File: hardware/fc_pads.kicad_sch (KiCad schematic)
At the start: 41 parts, among them J15 5V, J16 5V, J17 GND, J18 GND, J19 ADC2, J20 LED, J21 LED, J22 GND, J23 SCL, J24 5V, J25 5V, J26 SDA, J27 GND, J28 GND, J29 BUZ-, J30 5V, J31 LED, J32 LED, J33 BUZ+, J34 GND, J35 GND, J37 5V, J38 CAM, J39 VTX, J40 GND, J41 10V, J42 4V5, J43 GND, J44 PIO_TX0, J45 PIO_RX0, J46 NC, J47 NC, J48 RX0, J49 TX0, J50 GND, J51 GND, J52 4V5, J53 GND, J54 TX1, J55 RX1, U12 SM06B-SRSS-TB(LF)(SN)

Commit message: Schematic readability: TP texts, C19/C107, C26, title blocks (FB5 item 6, V9-V11/M6)
- TestPoint values ('TestPoint') hidden on all sheets: the stacked TP16/TP17
  (root), TP24/TP25 and TP18/TP19/TP26/TP27 (RP2354A) texts no longer overlap.
- C19 reference/value moved left of the part (no longer printed over C107).
- C26 Description field hidden.
- Title blocks: rev r2, date 2026-10 (title added where missing) on the root,
  RP2354A, Power, IMU, OSD, Pads, ESC channel and Core interface sheets.
Edited with kicad-skip, re-saved with `kicad-cli sch upgrade --force` so the
diff stays minimal. Not done: rx_esp32c3_sx1281 and fc_blackbox title blocks
(they carry other projects' instances, OpenRX-Lite / BLACKBOX, and the headless
re-save renumbers their references); TP10 outside the frame (moving it would
detach its wire); N4 SPI0 label lift (label position is the connection point);
M7 net naming (+4v5 / +3.3V vs +3V3) left as is, it touches the LGA spec.
ERC 31 errors (unchanged).

Co-Authored-By: Claude Opus 5.5 <noreply@anthropic.com>
Claude-Session: https://claude.ai/code/session_01KTp3FLjVXfXdWrkmr6af7d
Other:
- title: (none) -> Pads
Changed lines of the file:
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@@
 	(generator_version "10.0")
 	(paper "A4")
+	(title_block
+		(title "Pads")
+		(date "2026-10")
+		(rev "r2")
+	)
 	(polyline
 		(pts

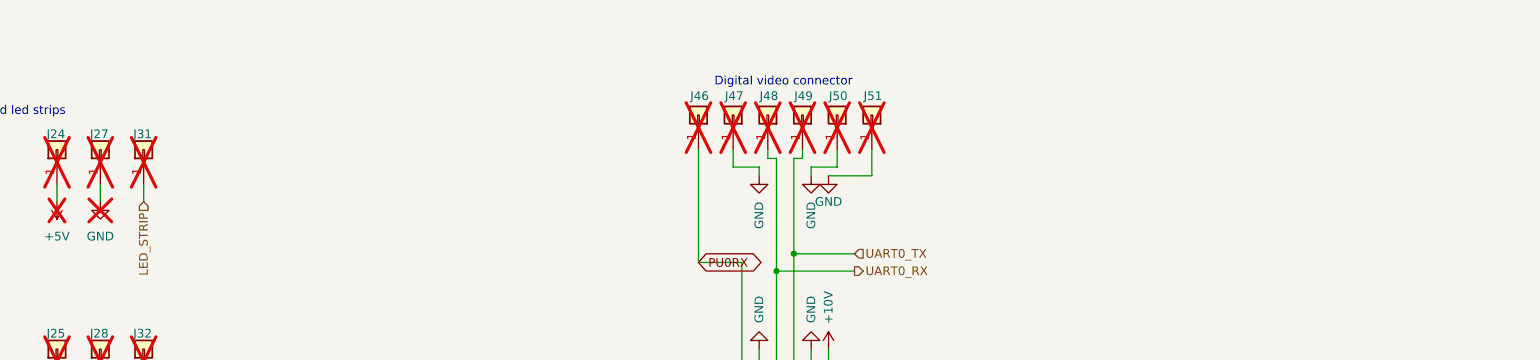
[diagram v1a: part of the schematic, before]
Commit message: One board: merge Base and Core onto the OpenAIO-Whoop 8L HDI stackup
- hardware/OpenAIO.kicad_pcb: the routed Base and Core layouts of 8fa8d7b
  side by side in one board, all routing kept (Core promoted to 8 layers
  before the append so no Base layer was dropped). J90/J91 LGA deleted;
  their 46 nets are now direct links (51 unconnected, listed in
  research/ROUTING.md). Stackup and board setup from OpenAIO-Whoop:
  8L HDI 1+6+1, 0.997 mm, 1 oz all layers, microvia 0.25/0.10,
  buried 0.33/0.15. Base DRC severities and exclusions kept.
- hardware/OpenAIO.kicad_dru: canonical block, Whoop HDI via rules,
  Base/Core rules that still apply; LGA, 2 oz and 1.6 mm via rules gone.
- Schematic: core_interface sheet removed; DPS368 baro U28 on I2C0;
  review fixes (U3 HF cap C116, RP2354 caps C117/C118, buzzer flyback D10,
  SD card on +3.3V, D9 on +4v5, FLASH_CS -> SD_CS, PWR_FLAGs, U7 pin
  names, ESC cap pin types, L4 LCSC). ERC 32 -> 0 errors.
- Libraries project-local: every footprint, 3D model and symbol in lib;
  OPENDRONE_LIB aliases removed from the lib tables.
- Two-board projects, multiboard config and LGA tools removed; Whoop
  board tools added in hardware/tools.
- Docs: README, AGENTS.md, research/ROUTING.md (hand-over),
  SCHEMATIC-REVIEW-2026-10-15.md, Betaflight target baro.

DRC: 38 errors (25 dangling LGA escape vias, 13 Core leftovers listed),
51 unconnected (the Base-Core links), 0 net or value parity issues.

Co-Authored-By: Claude Opus 5.5 <noreply@anthropic.com>
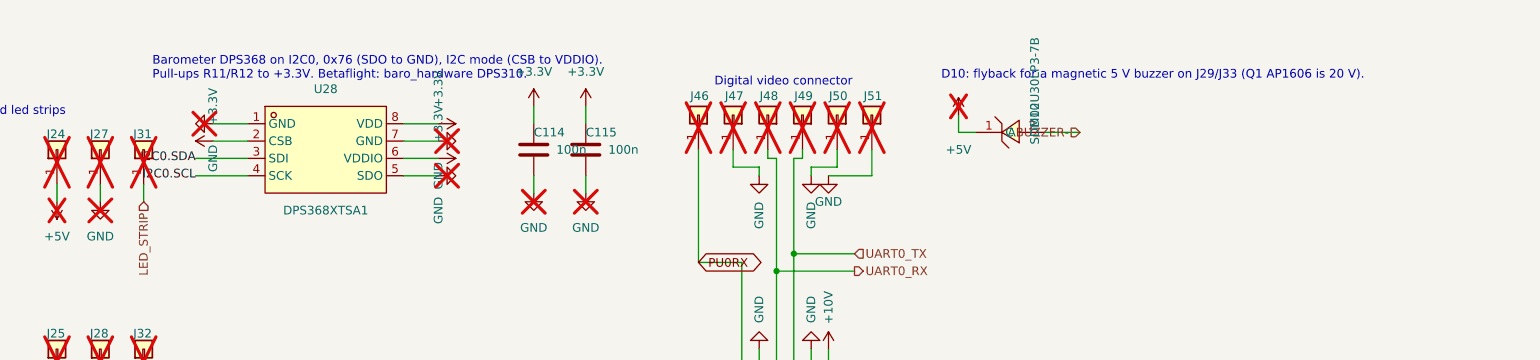
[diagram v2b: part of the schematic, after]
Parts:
- added C114, C115: 100n, lib:C_0201_0603Metric, symbol Device:C
- added D10: SDM02U30LP3-7B, lib:X3-DFN0603-2_L0.6-W0.3-RD, symbol lib:SDM02U30LP3-7B
- added U28: DPS368XTSA1, lib:LGA-8_L2.5-W2.0-P0.65-TR_DPS368, symbol lib:DPS368XTSA1
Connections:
- net +5V: now also D10.1 (C)
- net BUZZER-: now also D10.2 (A)
- net GND: now also C114.2, C115.2, U28.1 (GND), U28.5 (SDO), U28.7 (GND)
- net I2C0.SCL: now also U28.4 (SCK)
- net I2C0.SDA: now also U28.3 (SDI)
- new net +3.3V: C114.1, C115.1, U28.2 (CSB), U28.6 (VDDIO), U28.8 (VDD)
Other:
- note added: "Barometer DPS368 on I2C0, 0x76 (SDO to GND), I2C mode (CSB to VDDIO). Pull-ups R11/R12 to +3.3V. Betaflight: baro_hardware DPS310."
- note added: "D10: flyback for a magnetic 5 V buzzer on J29/J33 (Q1 AP1606 is 20 V)."

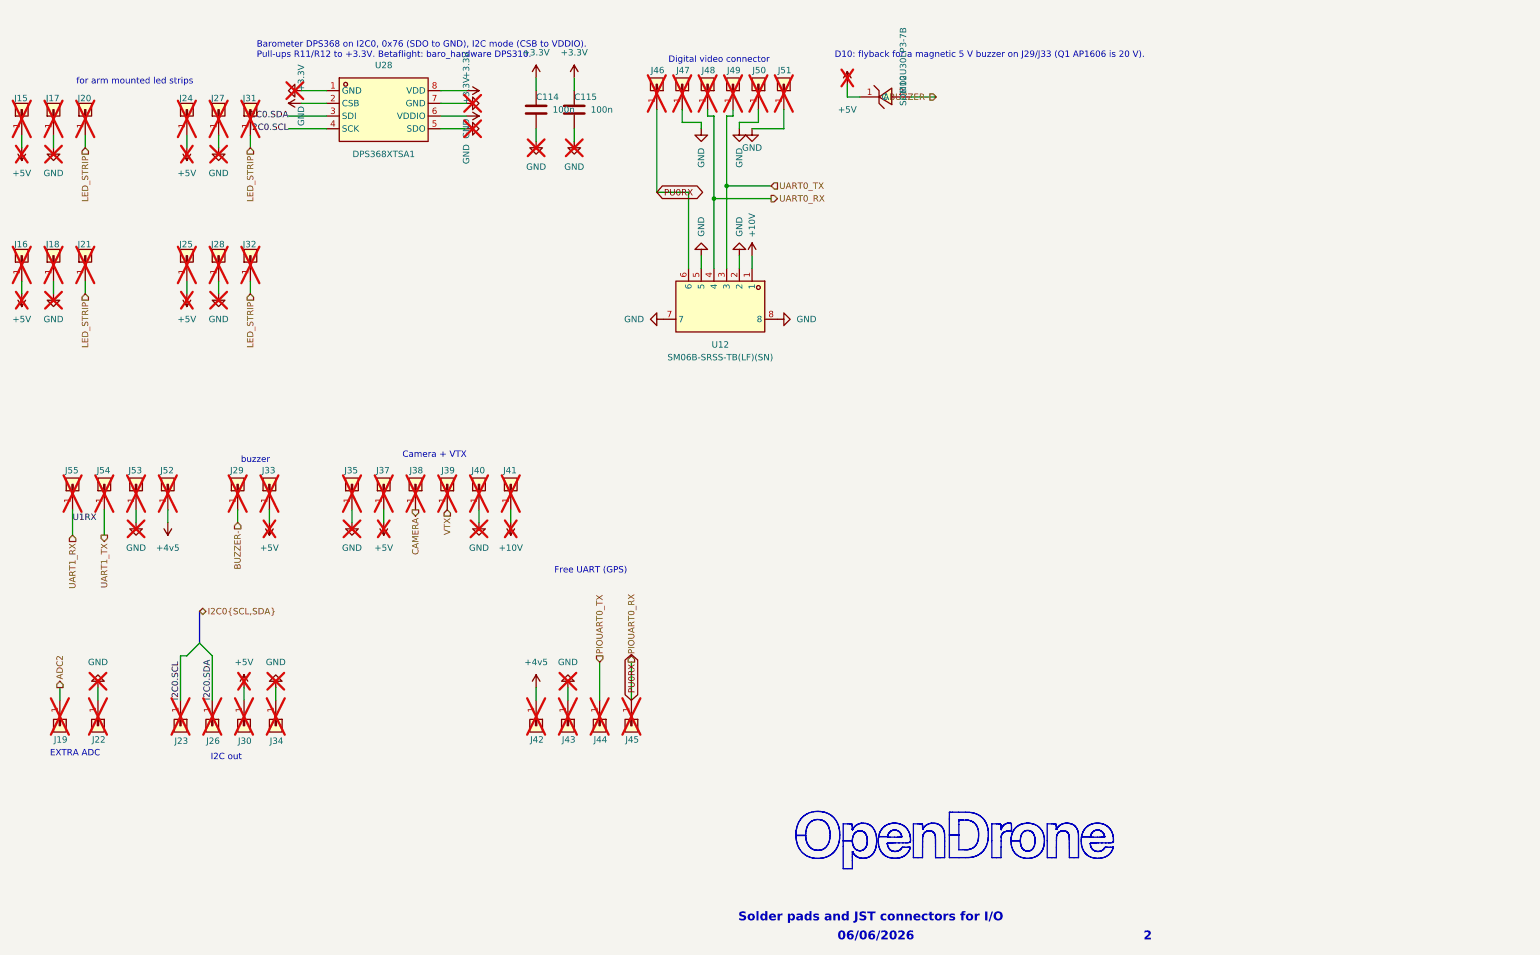
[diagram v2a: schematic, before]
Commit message: One board from the owner's 2026-08-22 Base and Core, BMP580 baro (#26)
The board is rebuilt from d81e559 (the hand-routed Base recovered from KiCad
local history and the hand-routed Core of 1fe3d21) plus the always-on +10V of
9aba717, instead of the agent-reworked 8fa8d7b. Both layouts sit side by side
in hardware/OpenAIO.kicad_pcb with all routing kept (2513 tracks, 1577 vias),
on the OpenAIO-Whoop 8L HDI stackup.

- Schematic: Core_Interface (J90/J91 LGA) removed; U26 BMP580 + C107/C108 on
  I2C0 at 0x47 (Betaflight BMP5xx default). Netlist otherwise identical to
  9aba717; ERC 31 errors, the 9aba717 baseline.
- Board: Base netclasses and severities; rule area "Core layout" keeps the
  Core's 0.09 line standard. DRC: 3 errors (USB1 peg), 37 unconnected (links).
- lib.pretty footprints replaced by the board instances; BMP580 imported with
  easyeda2kicad (LCSC C22391138).
- Not carried from 8fa8d7b: TXU0101 LED-strip buffer, +3V3_ESC, SWD pads,
  DFM edits; firmware ISSUES I2/I3 reopened.
- Docs: README pinout re-measured, AGENTS.md, research/ROUTING.md, Betaflight
  target USE_BARO_BMP580.

Co-authored-by: Stan <stan@openaio.local>
Co-authored-by: Claude Opus 5.5 <noreply@anthropic.com>
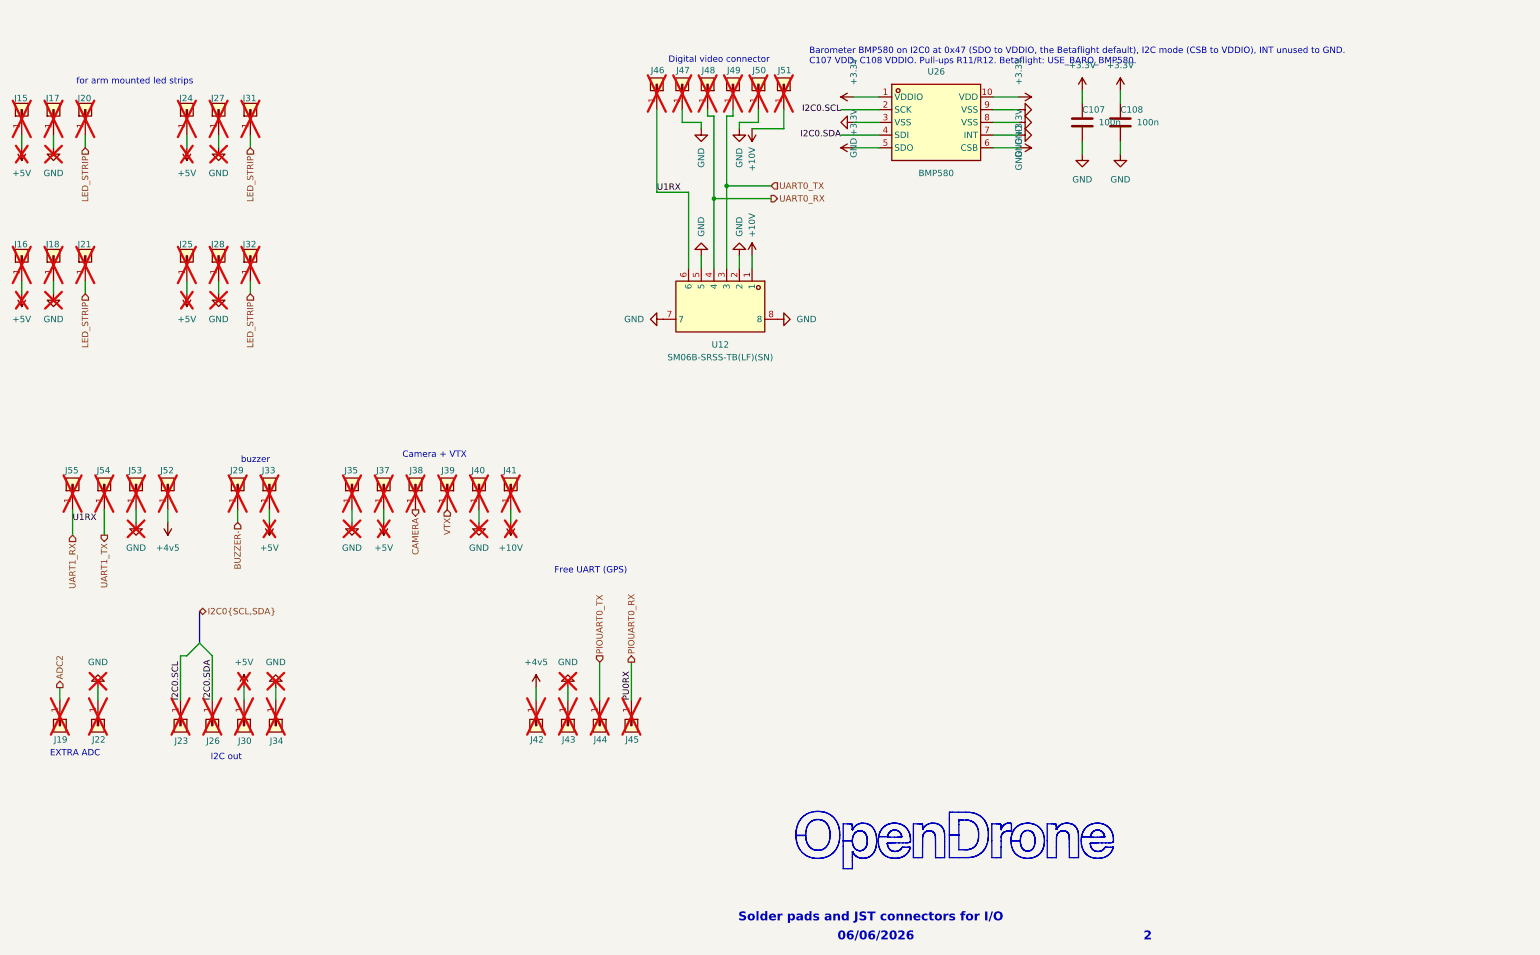
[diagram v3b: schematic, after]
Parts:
- removed C114, C115: 100n, lib:C_0201_0603Metric, symbol Device:C
- removed D10: SDM02U30LP3-7B, lib:X3-DFN0603-2_L0.6-W0.3-RD, symbol lib:SDM02U30LP3-7B
- removed U28: DPS368XTSA1, lib:LGA-8_L2.5-W2.0-P0.65-TR_DPS368, symbol lib:DPS368XTSA1
- added C107, C108: 100n, lib:C_0201_0603Metric, symbol Device:C
- added U26: BMP580, lib:LGA-10_L2.0-W2.0-P0.50-TL_BMP580, symbol lib:BMP580
- J17, J18, J22, J27, J28, J34, J35, J40, J43, J50, J53: value GND -> 5V
- J19: value ADC2 -> 5V
- J20, J21, J31, J32: value LED -> 5V
- J23: value SCL -> 5V
- J26: value SDA -> 5V
- J29: value BUZ- -> 5V
- J33: value BUZ+ -> 5V
- J38: value CAM -> 5V
- J39: value VTX -> 5V
- J41: value 10V -> 5V; footprint lib:SolderPad_1.2x1.2mm -> lib:small_pad
- J42, J52: value 4V5 -> 5V
- J44: value PIO_TX0 -> 5V
- J45: value PIO_RX0 -> 5V
- J46, J47: value NC -> 5V
- J48: value RX0 -> 5V
- J49: value TX0 -> 5V
- J51: value GND -> 5V; footprint lib:SolderPad_1.2x1.2mm -> lib:small_pad
- J54: value TX1 -> 5V
- J55: value RX1 -> 5V
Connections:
- net +10V: now also J51.1 (Pin_1)
- net +3.3V: now also C107.1, C108.1, U26.1 (VDDIO), U26.10 (VDD), U26.5 (SDO), U26.6 (CSB)
- net GND: now also C107.2, C108.2, U26.3 (VSS), U26.7 (INT), U26.8 (VSS), U26.9 (VSS); no longer J51.1 (Pin_1)
- net I2C0.SCL: now also U26.2 (SCK)
- net I2C0.SDA: now also U26.4 (SDI)
- net UART1_RX: now also J46.1 (Pin_1), U12.6
- removed net PU0RX: J45.1 (Pin_1), J46.1 (Pin_1), U12.6
- new net PIOUART0_RX: J45.1 (Pin_1)
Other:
- note added: "Barometer BMP580 on I2C0 at 0x47 (SDO to VDDIO, the Betaflight default), I2C mode (CSB to VDDIO), INT unused to GND. C107 VDD, C108 VDDIO. Pull-ups R11/R12. Betaflight: USE_BARO_BMP580."
- note removed: "Barometer DPS368 on I2C0, 0x76 (SDO to GND), I2C mode (CSB to VDDIO). Pull-ups R11/R12 to +3.3V. Betaflight: baro_hardware DPS310."
- note removed: "D10: flyback for a magnetic 5 V buzzer on J29/J33 (Q1 AP1606 is 20 V)."
- title: Pads -> (none)

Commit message: Library: every symbol, footprint and 3D model project-local (#28)
* Owner: board cleanup, Core placed on the board

Co-Authored-By: Claude Opus 5.5 <noreply@anthropic.com>

* Library: every symbol, footprint and 3D model project-local

- 3D models: 275 board model paths and 28 lib.pretty footprints pointed at
  KiCad's stock install or at ${OPENDRONE_LIB} (which this machine's KiCad sets
  to a path that does not exist, so 9 models were missing). All now resolve to
  ${KIPRJMOD}/lib.3dshapes; the three missing ones come from the repo's
  KiCad-Library submodule. .wrl replaced by the .step sibling where one exists.
- Symbols: the 14 stock symbols (Device, power, Connector, Connector_Generic,
  MCU_Espressif) copied into lib.kicad_sym from the schematic's own cache and
  relinked as lib:. Four lib symbols refreshed from the schematic (they still
  held the 8fa8d7b copies).
- Pruned: 11 unused footprints, 7 unused symbols, unreferenced model files.
- tools/localise_models.py and tools/localise_symbols.py keep it that way.
- Checks: board diff is model lines only; netlist identical; ERC 31 errors as
  before, lib_symbol_mismatch 9 -> 0.

Co-Authored-By: Claude Opus 5.5 <noreply@anthropic.com>

---------

Co-authored-by: Stan <stan@openaio.local>
Co-authored-by: Claude Opus 5.5 <noreply@anthropic.com>
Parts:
- C107, C108: symbol Device:C -> lib:C
- J15, J16, J17, J18, J19, J20, J21, J22, J23, J24, J25, J26, J27, J28, J29, J30, J31, J32, J33, J34, J35, J37, J38, J39, J40, J41, J42, J43, J44, J45, J46, J47, J48, J49, J50, J51, J52, J53, J54, J55: symbol Connector_Generic:Conn_01x01 -> lib:Conn_01x01

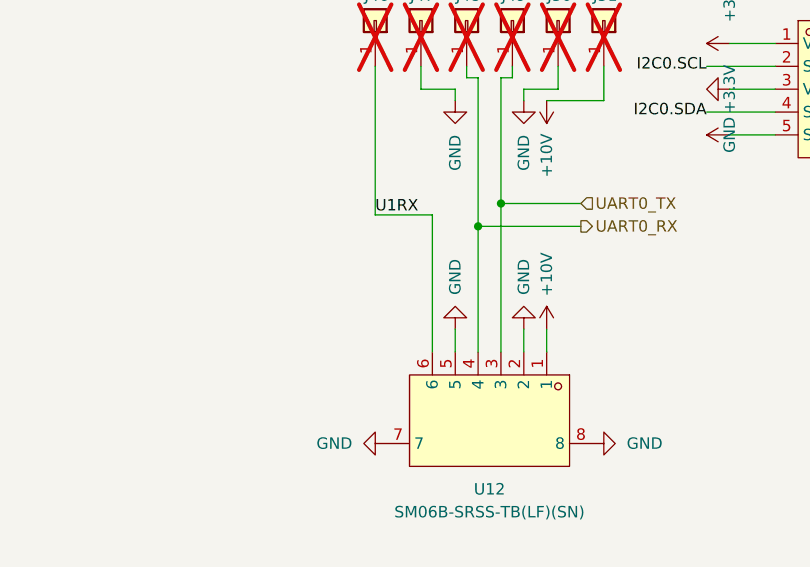
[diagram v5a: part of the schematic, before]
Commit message: IO remap: shortest RP2354A runs on the placed board; SBUS back on UART0
tools/io_opt.py (constraint-checked assignment, research/IO-CONSTRAINTS.md)
picked the mapping; tools/io_remap_sch.py edits the sheets (sexpdata),
re-saved with kicad-cli; netlist diff shows only the intended pins changed.

| Net | GPIO before | GPIO after |
|---|---|---|
| MOTOR2 | 24 | 21 |
| MOTOR3 | 23 | 18 |
| MOTOR4 | 22 | 8 |
| SPI0.SCK (SD) | 18 | 22 |
| FLASH_CS (SD CS) | 21 | 24 |
| LED_STRIP_L | 8 | 26 |
| LED0 | 26 | 27 |
| free | 27 | 23 |

U2-to-part distance 147.2 -> 136.5 mm; UART, I2C, SPI1, OSD, ADC unchanged.
SH-6 pin 6 (air unit SBUS) moved from UART1_RX, where it fought the ESP32
TX, to PU0RX (hardware UART0 RX, GPIO3) as config.h intends.
Board: pad nets synced, 2.3 mm UART1_RX stub at U12.6 removed.
DRC 0 errors, unconnected 78 -> 79 (U12.6 to PU0RX to route).
config.h and PINOUT.md updated.

Co-Authored-By: Claude Opus 5.5 <noreply@anthropic.com>
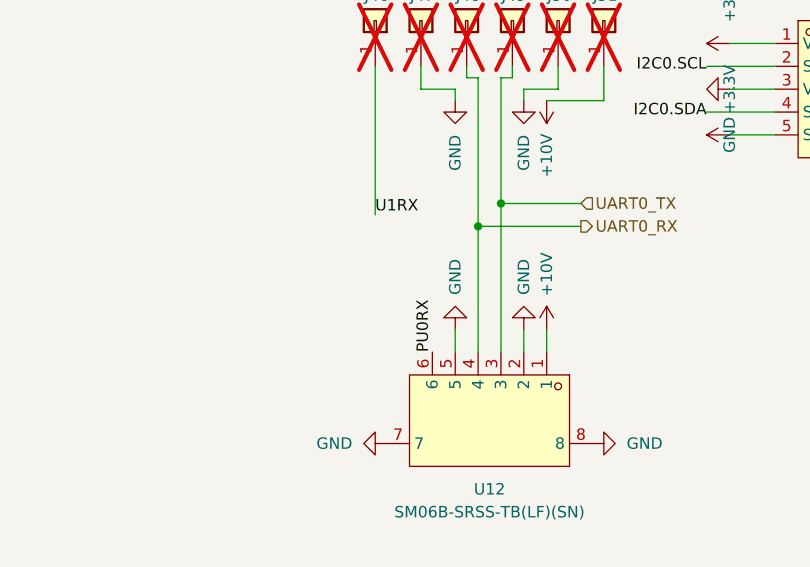
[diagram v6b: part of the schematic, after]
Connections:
- net PIOUART0_RX: now also U12.6
- net UART1_RX: no longer U12.6
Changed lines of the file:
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@@
-	(wire
-		(pts
-			(xy 172.72 44.45) (xy 179.07 44.45)
-		)
-		(stroke
-			(width 0)
-			(type default)
-		)
-	)
 	(wire
 		(pts
@@
 		(pts
 			(xy 217.17 35.56) (xy 212.09 35.56)
-		)
-		(stroke
-			(width 0)
-			(type default)
-		)
-	)
-	(wire
-		(pts
-			(xy 179.07 44.45) (xy 179.07 59.69)
 		)
 		(stroke
@@
 		(effects
 			(font
+				(size 1.27 1.27)
+			)
+			(justify left bottom)
+		)
+	)
+	(label "PU0RX"
+		(at 179.07 59.69 90)
+		(effects
+			(font

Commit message: Revert the IO remap and SH-6 pin 6 change: the owner's routing stays
The pins were routed meanwhile; with that routing counted as rework the
optimiser keeps today's mapping. SBUS on the ELRS RX line is the owner's
choice (ELRS unused when the DJI receiver is). Kept: tools/io_opt.py,
tools/io_remap_sch.py and research/IO-CONSTRAINTS.md for later use.

Co-Authored-By: Claude Opus 5.5 <noreply@anthropic.com>
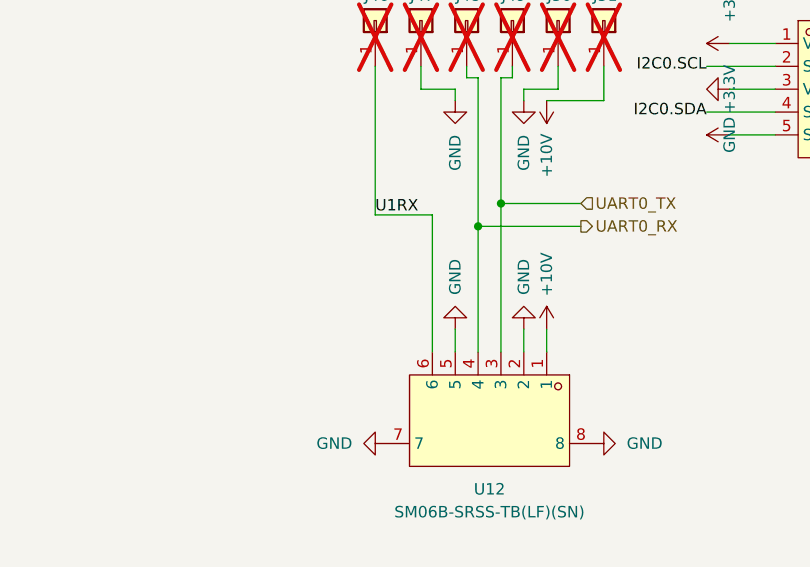
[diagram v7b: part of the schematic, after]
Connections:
- net PIOUART0_RX: no longer U12.6
- net UART1_RX: now also U12.6
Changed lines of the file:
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@@
+	(wire
+		(pts
+			(xy 172.72 44.45) (xy 179.07 44.45)
+		)
+		(stroke
+			(width 0)
+			(type default)
+		)
+	)
 	(wire
 		(pts
@@
 		(pts
 			(xy 217.17 35.56) (xy 212.09 35.56)
+		)
+		(stroke
+			(width 0)
+			(type default)
+		)
+	)
+	(wire
+		(pts
+			(xy 179.07 44.45) (xy 179.07 59.69)
 		)
 		(stroke
@@
 		(effects
 			(font
-				(size 1.27 1.27)
-			)
-			(justify left bottom)
-		)
-	)
-	(label "PU0RX"
-		(at 179.07 59.69 90)
-		(effects
-			(font
